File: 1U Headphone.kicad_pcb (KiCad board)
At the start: 2 copper layers, 57.2 x 28.6 mm, 35 parts, among them J1 L IN, J2 R IN, J3 OUT, J4 Header_1x05, J5 Header_1x05, J6 Header_1x03, P1 A50k, U1 NJM2068

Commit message: Changed everything
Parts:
- removed MH1, MH2: MountingHole, Mounting_Holes:MountingHole_3.2mm_M3
- removed P1: A50k, MojaBiblioteka:POT-9MM-ALPHA-DUAL
- removed R17, R18: R, Resistors_SMD:R_0805_HandSoldering
- removed S1: SPDT, 4ms-footprints:SPDT-SUB
- added C11: 100n, Capacitor_SMD:C_0603_1608Metric_Pad1.05x0.95mm_HandSolder, F.Cu at (55.6, 66.2)
- added C12: 100n, Capacitor_SMD:C_0603_1608Metric_Pad1.05x0.95mm_HandSolder, F.Cu at (48.5, 73.7)
- added C13: 100n, Capacitor_SMD:C_0603_1608Metric_Pad1.05x0.95mm_HandSolder, F.Cu at (70.4, 66.2)
- added C14: 100n, Capacitor_SMD:C_0603_1608Metric_Pad1.05x0.95mm_HandSolder, F.Cu at (63.1, 73.7)
- added D3: LED, LED_THT:LED_D3.0mm, B.Cu at (33.8, 62.4)
- added D4: LED, LED_THT:LED_D3.0mm, B.Cu at (27.9, 62.4)
- added J10: POT_L_M, Connector_PinHeader_2.54mm:PinHeader_1x03_P2.54mm_Vertical, B.Cu at (67.9, 62.4)
- added J7: POT_R_C, Connector_PinSocket_2.54mm:PinSocket_1x03_P2.54mm_Vertical, F.Cu at (24.6, 62.4)
- added J8: POT_R_M, Connector_PinHeader_2.54mm:PinHeader_1x03_P2.54mm_Vertical, B.Cu at (53.7, 62.4)
- added J9: POT_L_C, Connector_PinSocket_2.54mm:PinSocket_1x03_P2.54mm_Vertical, F.Cu at (38.9, 62.4)
- added Q1: MMBT3904, Package_TO_SOT_SMD:SOT-23, F.Cu at (35.1, 73.7)
- added Q2: MMBT3904, Package_TO_SOT_SMD:SOT-23, F.Cu at (38.8, 73.7)
- added R11: 75, Resistor_SMD:R_0603_1608Metric_Pad1.05x0.95mm_HandSolder, F.Cu at (58.6, 69.4)
- added R12: 75, Resistor_SMD:R_0603_1608Metric_Pad1.05x0.95mm_HandSolder, F.Cu at (73.3, 69.4)
- added R14: 1k, Resistor_SMD:R_0603_1608Metric_Pad1.05x0.95mm_HandSolder, F.Cu at (28.2, 65.9)
- added R16: 100k, Resistor_SMD:R_0603_1608Metric_Pad1.05x0.95mm_HandSolder, F.Cu at (44.2, 69.8)
- added R7: 10k, Resistor_SMD:R_0603_1608Metric_Pad1.05x0.95mm_HandSolder, F.Cu at (48.5, 67.5)
- added R8: 10k, Resistor_SMD:R_0603_1608Metric_Pad1.05x0.95mm_HandSolder, F.Cu at (63.1, 67.8)
- added RV1: 100k, KraakenStuff:POT-9MM-ALPHA, B.Cu at (24.4, 53.1)
- added RV2: 100k, KraakenStuff:POT-9MM-ALPHA, B.Cu at (39.1, 53.1)
- added U2: NE5532, Package_SO:SOIC-8_3.9x4.9mm_P1.27mm, F.Cu at (53.5, 70.4)
- added U3: NE5532, Package_SO:SOIC-8_3.9x4.9mm_P1.27mm, F.Cu at (68.3, 70.5)
- added ~: Perforacija, KraakenStuff:Perforacija, F.Cu at (46.3, 63.0)
- C1, C2: value 100n -> 10p; footprint Capacitors_THT:C_Rect_L7.2mm_W2.5mm_P5.00mm_FKS2_FKP2_MKS2_MKP2 -> Capacitor_SMD:C_0603_1608Metric_Pad1.05x0.95mm_HandSolder
- C10, C9: footprint Capacitors_SMD:C_0603_HandSoldering -> Capacitor_SMD:C_0603_1608Metric_Pad1.05x0.95mm_HandSolder
- C3, C4: value 100n -> 10uF; footprint Capacitors_THT:C_Rect_L7.2mm_W2.5mm_P5.00mm_FKS2_FKP2_MKS2_MKP2 -> Capacitor_SMD:CP_Elec_4x5.7
- C5, C6: value 100n -> 10uF; footprint Capacitors_SMD:C_0603_HandSoldering -> Capacitor_SMD:CP_Elec_4x5.7
- C7, C8: value 100u -> 100n; footprint Capacitors_SMD:CP_Elec_6.3x7.7 -> Capacitor_SMD:C_0603_1608Metric_Pad1.05x0.95mm_HandSolder
- D1, D2: footprint Diodes_SMD:D_SOD-123 -> Diode_SMD:D_SOD-123
- J1: value L IN -> R_IN; footprint 4ms-footprints:PJ301M-12 -> KraakenStuff:PJ301M-12; moved to B.Cu
- J2: value R IN -> L_IN; footprint 4ms-footprints:PJ301M-12 -> KraakenStuff:PJ301M-12; moved to B.Cu
- J3: footprint MojaBiblioteka:PJ366ST -> KraakenStuff:PJ366ST; moved to B.Cu
- J4: value Header_1x05 -> PWR; footprint MojaBiblioteka:Header 1x5 -> Connector_PinHeader_2.54mm:PinHeader_1x03_P2.54mm_Vertical; moved to F.Cu
- J5: value Header_1x05 -> PWR_C; footprint MojaBiblioteka:Header 1x5 -> Connector_PinSocket_2.54mm:PinSocket_1x03_P2.54mm_Vertical
- J6: value Header_1x03 -> PWR_M; footprint MojaBiblioteka:Header 1x3 -> Connector_PinHeader_2.54mm:PinHeader_1x03_P2.54mm_Vertical
- R1, R2: value R -> 100k; footprint Resistors_SMD:R_0805_HandSoldering -> Resistor_SMD:R_0603_1608Metric_Pad1.05x0.95mm_HandSolder
- R10, R9: value R -> 75; footprint Resistors_SMD:R_0805_HandSoldering -> Resistor_SMD:R_0603_1608Metric_Pad1.05x0.95mm_HandSolder; moved to F.Cu
- R13: value 68R/0.5W -> 1k; footprint Resistors_SMD:R_0805_HandSoldering -> Resistor_SMD:R_0603_1608Metric_Pad1.05x0.95mm_HandSolder; moved to F.Cu
- R15: value 68R/0.5W -> 100k; footprint Resistors_SMD:R_0805_HandSoldering -> Resistor_SMD:R_0603_1608Metric_Pad1.05x0.95mm_HandSolder; moved to F.Cu
- R3, R4: value 100k -> 39k; footprint Resistors_SMD:R_0805_HandSoldering -> Resistor_SMD:R_0603_1608Metric_Pad1.05x0.95mm_HandSolder
- R5, R6: value R -> 10k; footprint Resistors_SMD:R_0805_HandSoldering -> Resistor_SMD:R_0603_1608Metric_Pad1.05x0.95mm_HandSolder; moved to F.Cu
- U1: value NJM2068 -> TL072; footprint 4ms-footprints:DMP8 -> Package_SO:TSSOP-8_4.4x3mm_P0.65mm; moved to F.Cu
- moved C4 214.5 mm to (24.4, 50.6), turned to 180 degrees
- moved J5 203.5 mm to (31.8, 56.9), turned to 180 degrees
- moved C2 199.7 mm to (36.0, 50.0)
- moved C3 194.2 mm to (24.4, 56.1), turned to 180 degrees
- moved R4 193.7 mm to (37.5, 50.0), turned to 90 degrees
- moved R15 191.3 mm to (39.0, 69.8), turned to 270 degrees
- moved R13 190.8 mm to (35.0, 65.9), turned to 90 degrees
- moved R3 186.0 mm to (37.5, 56.8), turned to 90 degrees
- moved U1 185.9 mm to (40.1, 53.9), turned to 90 degrees
- moved R2 185.2 mm to (44.2, 66.0)
- moved J3 181.9 mm to (22.4, 70.4)
- moved R1 180.5 mm to (39.0, 66.1)
- moved C1 177.8 mm to (36.0, 56.8), turned to 90 degrees
- moved C8 173.8 mm to (56.5, 51.8)
- moved C7 172.2 mm to (56.3, 57.0), turned to 0 degrees
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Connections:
- C1 pad 2: L_IN -> Net-(C1-Pad2)
- C2 pad 2: R_IN -> Net-(C2-Pad2)
- C3 pad 1: GND -> Net-(C1-Pad1)
- C4 pad 1: GND -> Net-(C2-Pad1)
- J4 pad 2: L_OUT -> Net-(D2-Pad2)
- J4 pad 3: R_OUT -> Net-(D1-Pad1)
- J5 pad 1: GND -> -12V
- J5 pad 2: L_OUT -> +12V
- J5 pad 3: R_OUT -> GND
- J6 pad 1: Net-(D2-Pad2) -> -12V
- J6 pad 2: GND -> +12V
- J6 pad 3: Net-(D1-Pad1) -> GND
- R1 pad 1: L_IN -> Net-(C1-Pad2)
- R1 pad 2: GND -> Net-(J1-PadT)
- R10 pad 1: GND -> OUT_L_M
- R13 pad 1: L_OUT -> Net-(Q1-Pad3)
- R13 pad 2: Net-(R13-Pad2) -> Net-(D3-Pad1)
- R15 pad 1: R_OUT -> Net-(J1-PadT)
- R15 pad 2: Net-(R15-Pad2) -> Net-(Q1-Pad1)
- R2 pad 1: R_IN -> Net-(C2-Pad2)
- R2 pad 2: GND -> Net-(J2-PadT)
- R3 pad 2: GND -> Net-(C1-Pad2)
- R4 pad 2: GND -> Net-(C2-Pad2)
- R5 pad 1: Net-(R13-Pad2) -> Net-(R5-Pad1)
- R5 pad 2: Net-(R5-Pad2) -> POT_R_M
- R6 pad 1: GND -> Net-(R6-Pad1)
- R6 pad 2: Net-(R5-Pad2) -> POT_L_M
- R9 pad 1: Net-(R15-Pad2) -> OUT_R_M
- R9 pad 2: Net-(R10-Pad2) -> Net-(R7-Pad1)
- U1 pad 1: Net-(R13-Pad2) -> Net-(C1-Pad1)
- U1 pad 2: Net-(R5-Pad2) -> Net-(C1-Pad2)
- U1 pad 3: Net-(C1-Pad1) -> GND
- U1 pad 4: -12V -> +12V
- U1 pad 5: Net-(C2-Pad1) -> GND
- U1 pad 6: Net-(R10-Pad2) -> Net-(C2-Pad2)
- U1 pad 7: Net-(R15-Pad2) -> Net-(C2-Pad1)
- U1 pad 8: +12V -> -12V
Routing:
- net +12V: track 32.9 -> 101.4 mm, vias 3 -> 0
- net L_OUT: track 61.2 -> 0.00 mm
- net L_IN: track 45.7 -> 0.00 mm, vias 1 -> 0
- net R_OUT: track 32.9 -> 0.00 mm
- net OUT_L_M: track 0.00 -> 31.9 mm, vias 0 -> 1
- net Net-(J3-Pad2): track 30.8 -> 0.00 mm
- net R_IN: track 28.1 -> 0.00 mm
- net GND: track 26.0 -> 0.00 mm, vias 5 -> 2
- net -12V: track 56.8 -> 82.8 mm, vias 5 -> 0
- net Net-(C2-Pad2): track 0.00 -> 24.4 mm, vias 0 -> 2
- net Net-(R13-Pad2): track 22.6 -> 0.00 mm
- net Net-(J1-Pad3): track 20.3 -> 0.00 mm
- net Net-(C3-Pad2): track 22.2 -> 4.26 mm, vias 1 -> 0
- net Net-(J1-PadT): track 0.00 -> 17.8 mm, vias 0 -> 2
- net Net-(C4-Pad2): track 3.73 -> 21.3 mm, vias 0 -> 1
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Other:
- board size 57.2 x 28.6 mm -> 57 x 28.7 mm
- net class Default: clearance 0.25 -> 0.2; trace_width 0.35 -> 0.25
- rule pad_to_mask_clearance: 0.2 -> 0
- rule trace_clearance: 0.25 -> 0.2
- board text added: "KraakenStuff Headphone v.0.1"
- board text removed: "Kraaken Headphone v0.1"

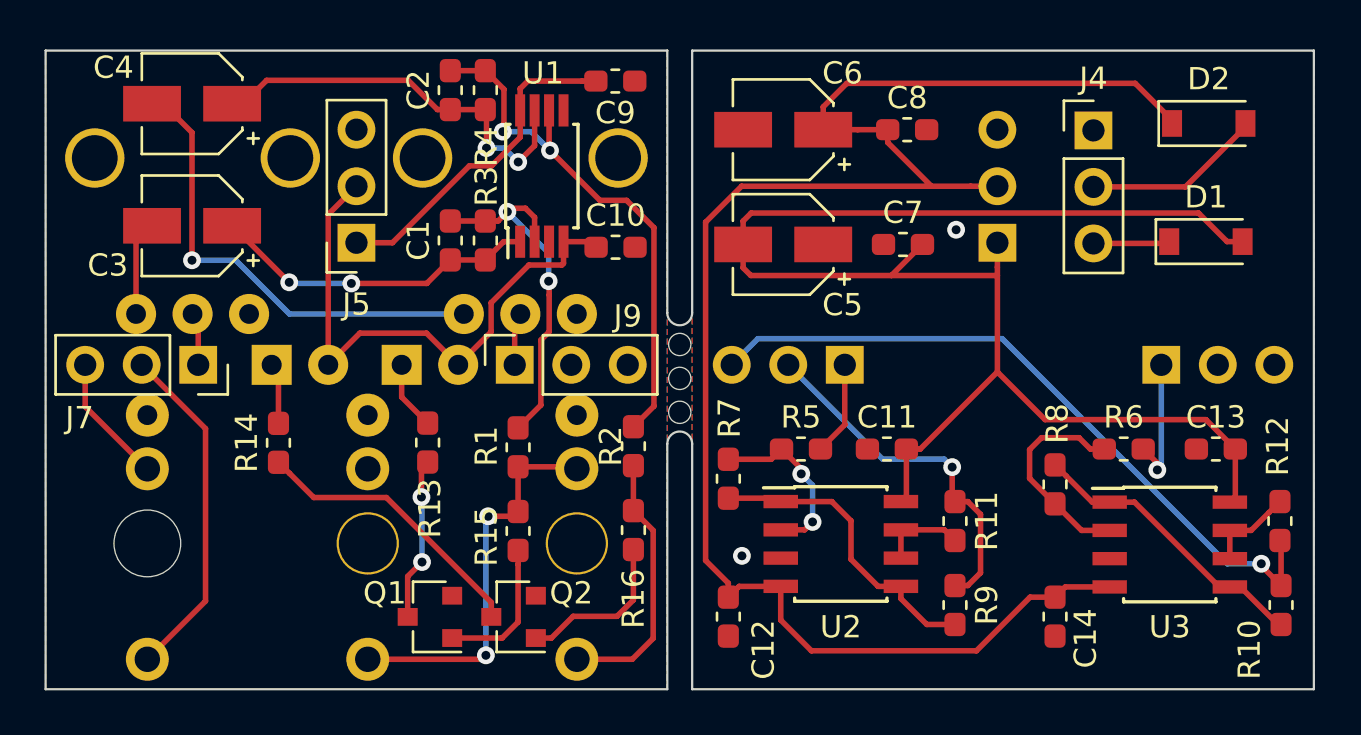
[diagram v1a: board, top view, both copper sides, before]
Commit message: Fixed error in powering op amps
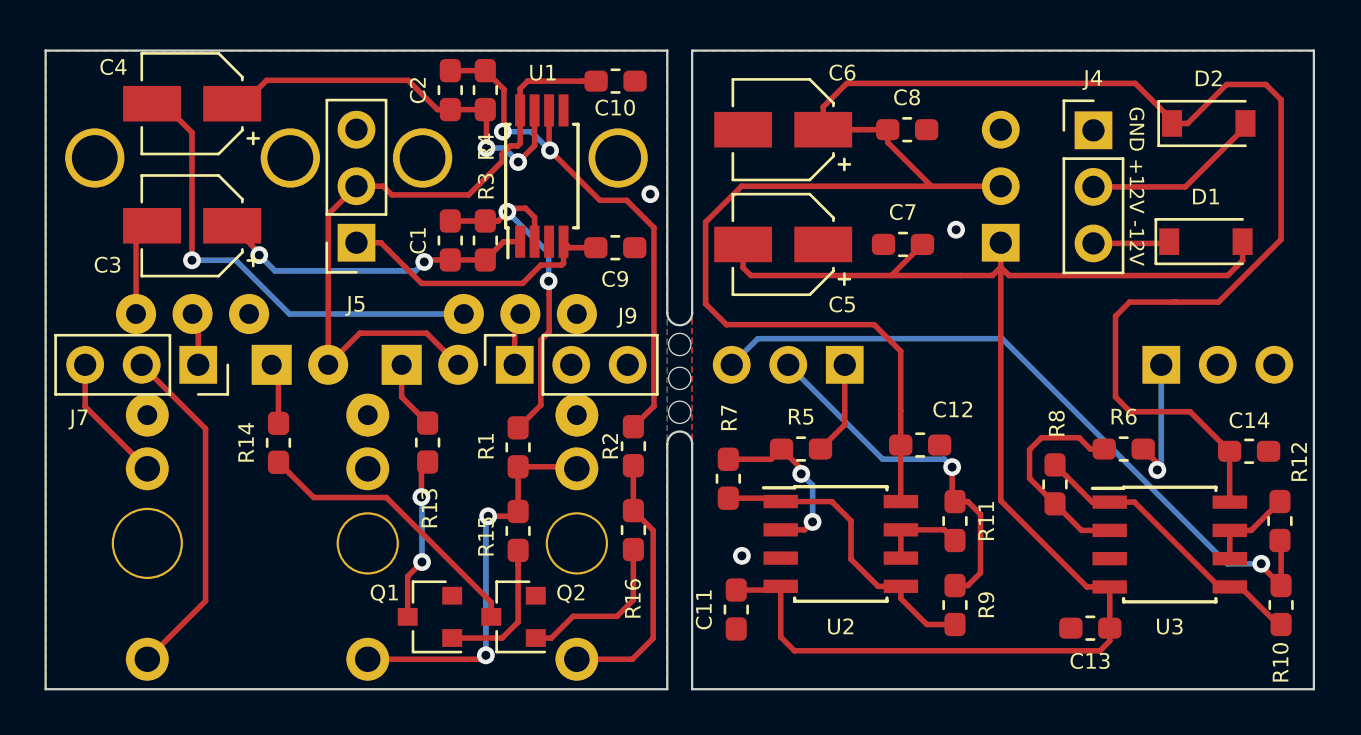
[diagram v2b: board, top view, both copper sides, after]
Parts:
- moved C12 11.6 mm to (57.1, 66.0), turned to 0 degrees
- moved C14 11.5 mm to (71.9, 66.3), turned to 0 degrees
- moved C11 9.89 mm to (48.8, 73.4), turned to 90 degrees
- moved C13 9.83 mm to (64.7, 74.2)
- moved C9 7.49 mm to (43.4, 57.1)
- moved C10 7.47 mm to (43.4, 49.6)
- moved J6 0.15 mm to (60.7, 56.9)
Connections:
- U1 pad 4: +12V -> -12V
- U1 pad 8: -12V -> +12V
- U2 pad 4: +12V -> -12V
- U2 pad 8: -12V -> +12V
- U3 pad 4: +12V -> -12V
- U3 pad 8: -12V -> +12V
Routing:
- net +12V: track 101.4 -> 121.8 mm
- net -12V: track 82.8 -> 81.2 mm
- net GND: vias 2 -> 3
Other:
- board text added: "GND +12V -12V"
- board text added: "KraakenStuff Headphone v.0.2"
- board text removed: "KraakenStuff Headphone v.0.1"
